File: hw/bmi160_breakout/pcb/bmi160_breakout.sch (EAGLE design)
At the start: 4 parts, among them CON1 B4B-ZR, U1 BMI160LGA14

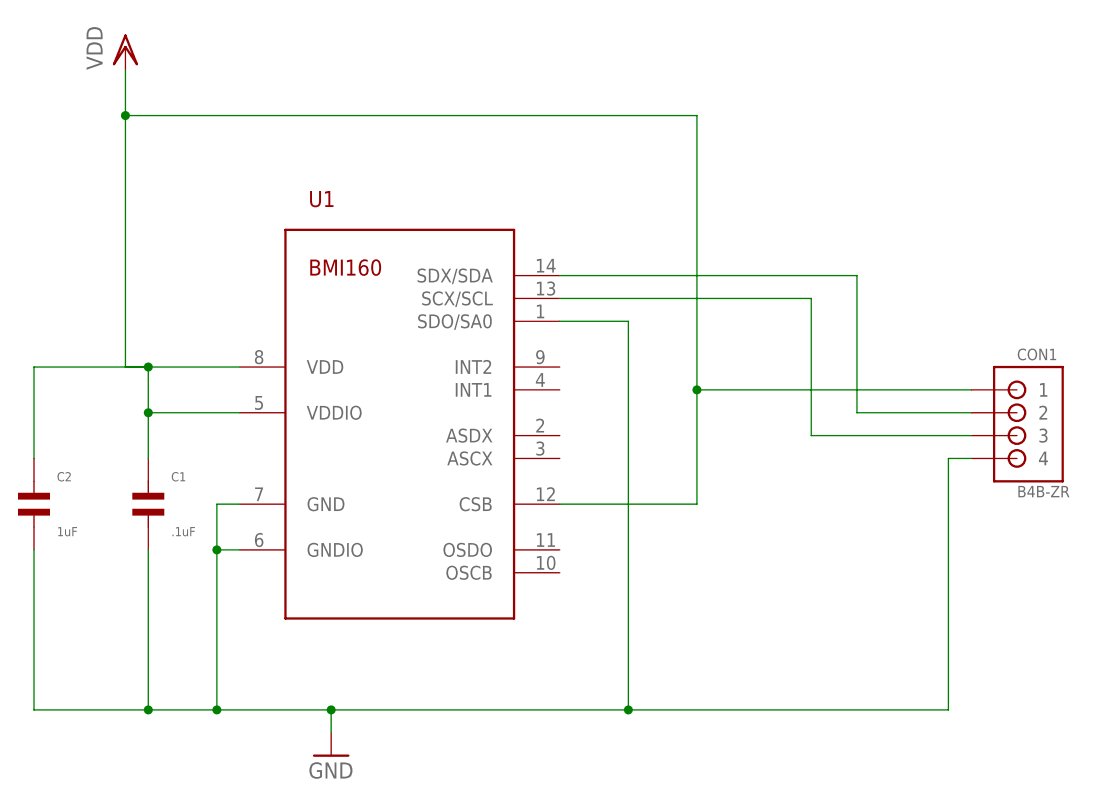
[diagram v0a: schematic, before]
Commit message: BMI160 breakout: Add a solder jumper to select I2C address.  Add silk to denote orientation.
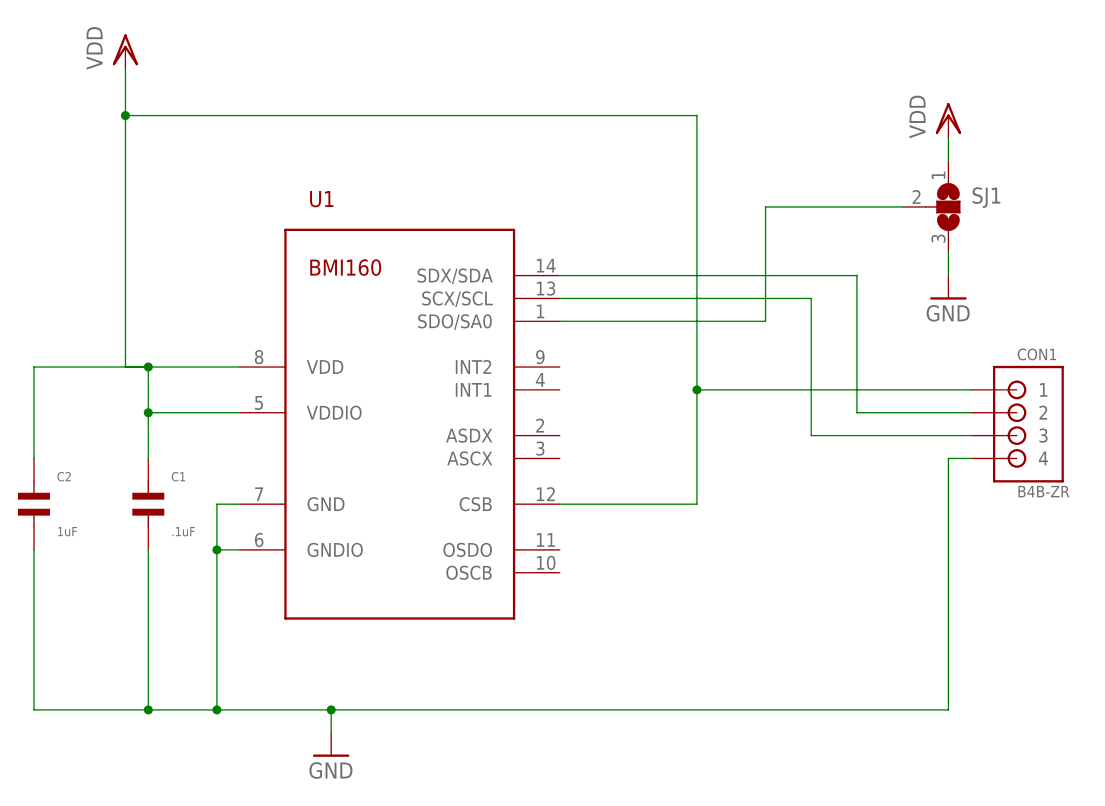
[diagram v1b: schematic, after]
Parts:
- added SJ1: (no value), jumper:SJ2W
- U1: MOUSER_PN (none) -> 262-BMI160; MPN (none) -> BMI160
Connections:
- new net N$1: SJ1.2, U1.SDO/SA0
- net GND: now also SJ1.3; no longer U1.SDO/SA0
- net VDD: now also SJ1.1
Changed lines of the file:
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@@
 </classes>
 <parts>
-<part name="U1" library="bmi160_breakout" deviceset="BMI160" device="LGA14"/>
+<part name="U1" library="bmi160_breakout" deviceset="BMI160" device="LGA14">
+<attribute name="MOUSER_PN" value="262-BMI160"/>
+<attribute name="MPN" value="BMI160"/>
+</part>
 <part name="GND1" library="supply1" deviceset="GND" device=""/>
 <part name="VDD1" library="supply1" deviceset="VDD" device=""/>
@@
 </part>
 <part name="CON1" library="bmi160_breakout" deviceset="B4B-ZR" device=""/>
+<part name="SJ1" library="jumper" deviceset="SJ2W" device=""/>
+<part name="GND2" library="supply1" deviceset="GND" device=""/>
+<part name="VDD2" library="supply1" deviceset="VDD" device=""/>
 </parts>
 <sheets>
@@
 </plain>
 <instances>
-<instance part="U1" gate="G$1" x="68.58" y="43.18"/>
+<instance part="U1" gate="G$1" x="68.58" y="43.18">
+<attribute name="MOUSER_PN" x="68.58" y="43.18" size="1.778" layer="96" display="off"/>
+<attribute name="MPN" x="68.58" y="43.18" size="1.778" layer="96" display="off"/>
+</instance>
 <instance part="GND1" gate="1" x="60.96" y="5.08"/>
 <instance part="VDD1" gate="G$1" x="38.1" y="83.82"/>
@@
 </instance>
 <instance part="CON1" gate="G$1" x="139.7" y="43.18"/>
+<instance part="SJ1" gate="G$1" x="129.54" y="66.04"/>
+<instance part="GND2" gate="1" x="129.54" y="55.88"/>
+<instance part="VDD2" gate="G$1" x="129.54" y="76.2"/>
 </instances>
 <busses>
@@
 <wire x1="27.94" y1="10.16" x2="40.64" y2="10.16" width="0.1524" layer="91"/>
 <junction x="40.64" y="10.16"/>
-<pinref part="U1" gate="G$1" pin="SDO/SA0"/>
-<wire x1="86.36" y1="53.34" x2="93.98" y2="53.34" width="0.1524" layer="91"/>
-<wire x1="93.98" y1="53.34" x2="93.98" y2="10.16" width="0.1524" layer="91"/>
-<wire x1="93.98" y1="10.16" x2="60.96" y2="10.16" width="0.1524" layer="91"/>
 <junction x="60.96" y="10.16"/>
-<wire x1="93.98" y1="10.16" x2="129.54" y2="10.16" width="0.1524" layer="91"/>
+<wire x1="60.96" y1="10.16" x2="129.54" y2="10.16" width="0.1524" layer="91"/>
 <wire x1="129.54" y1="10.16" x2="129.54" y2="38.1" width="0.1524" layer="91"/>
-<junction x="93.98" y="10.16"/>
 <pinref part="CON1" gate="G$1" pin="4"/>
 <wire x1="129.54" y1="38.1" x2="132.08" y2="38.1" width="0.1524" layer="91"/>
+</segment>
+<segment>
+<pinref part="SJ1" gate="G$1" pin="3"/>
+<pinref part="GND2" gate="1" pin="GND"/>
+<wire x1="129.54" y1="60.96" x2="129.54" y2="58.42" width="0.1524" layer="91"/>
 </segment>
 </net>
@@
 <junction x="101.6" y="45.72"/>
 </segment>
+<segment>
+<pinref part="SJ1" gate="G$1" pin="1"/>
+<pinref part="VDD2" gate="G$1" pin="VDD"/>
+<wire x1="129.54" y1="71.12" x2="129.54" y2="73.66" width="0.1524" layer="91"/>
+</segment>
 </net>
 <net name="SDA" class="0">
@@
 </segment>
 </net>
+<net name="N$1" class="0">
+<segment>
+<pinref part="U1" gate="G$1" pin="SDO/SA0"/>
+<wire x1="86.36" y1="53.34" x2="109.22" y2="53.34" width="0.1524" layer="91"/>
+<wire x1="109.22" y1="53.34" x2="109.22" y2="66.04" width="0.1524" layer="91"/>
+<pinref part="SJ1" gate="G$1" pin="2"/>
+<wire x1="109.22" y1="66.04" x2="124.46" y2="66.04" width="0.1524" layer="91"/>
+</segment>
+</net>

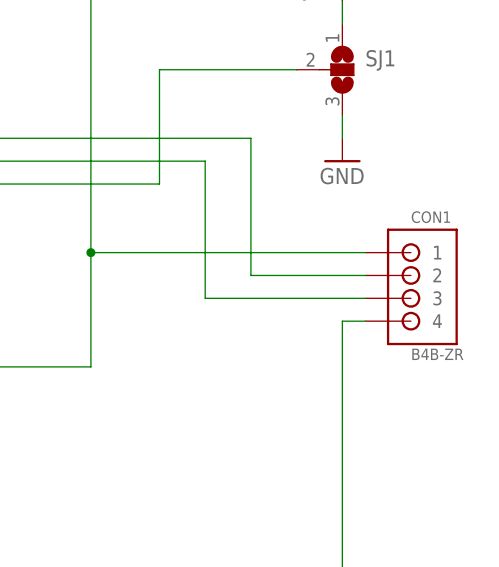
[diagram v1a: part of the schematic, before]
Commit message: bmi160 breakout: Update primary connector to 0.1" header, as it barely makes the board bigger but makes it a lot more convenient.
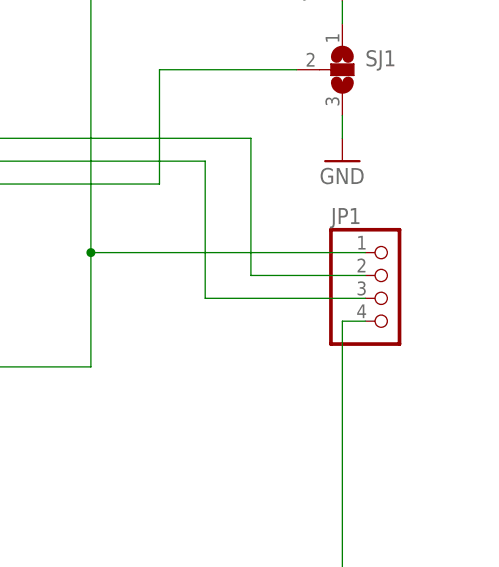
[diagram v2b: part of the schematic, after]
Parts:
- removed CON1: B4B-ZR, bmi160_breakout:B4B-ZR
- added JP1: (no value), pinhead:PINHD-1X4
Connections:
- net GND: now also JP1.4; no longer CON1.4
- net SCL: now also JP1.3; no longer CON1.3
- net SDA: now also JP1.2; no longer CON1.2
- net VDD: now also JP1.1; no longer CON1.1
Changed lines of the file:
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@@
 <attribute name="AMFPN" value="MF-CAP-0805-1uF"/>
 </part>
-<part name="CON1" library="bmi160_breakout" deviceset="B4B-ZR" device=""/>
 <part name="SJ1" library="jumper" deviceset="SJ2W" device=""/>
 <part name="GND2" library="supply1" deviceset="GND" device=""/>
 <part name="VDD2" library="supply1" deviceset="VDD" device=""/>
+<part name="JP1" library="pinhead" deviceset="PINHD-1X4" device=""/>
 </parts>
 <sheets>
@@
 <attribute name="AMFPN" x="27.94" y="33.02" size="1.778" layer="96" display="off"/>
 </instance>
-<instance part="CON1" gate="G$1" x="139.7" y="43.18"/>
 <instance part="SJ1" gate="G$1" x="129.54" y="66.04"/>
 <instance part="GND2" gate="1" x="129.54" y="55.88"/>
 <instance part="VDD2" gate="G$1" x="129.54" y="76.2"/>
+<instance part="JP1" gate="A" x="134.62" y="40.64"/>
 </instances>
 <busses>
@@
 <wire x1="60.96" y1="10.16" x2="129.54" y2="10.16" width="0.1524" layer="91"/>
 <wire x1="129.54" y1="10.16" x2="129.54" y2="38.1" width="0.1524" layer="91"/>
-<pinref part="CON1" gate="G$1" pin="4"/>
 <wire x1="129.54" y1="38.1" x2="132.08" y2="38.1" width="0.1524" layer="91"/>
+<pinref part="JP1" gate="A" pin="4"/>
 </segment>
 <segment>
@@
 <wire x1="101.6" y1="45.72" x2="101.6" y2="33.02" width="0.1524" layer="91"/>
 <wire x1="101.6" y1="33.02" x2="86.36" y2="33.02" width="0.1524" layer="91"/>
-<pinref part="CON1" gate="G$1" pin="1"/>
 <wire x1="132.08" y1="45.72" x2="101.6" y2="45.72" width="0.1524" layer="91"/>
 <junction x="101.6" y="45.72"/>
+<pinref part="JP1" gate="A" pin="1"/>
 </segment>
 <segment>
@@
 <wire x1="86.36" y1="58.42" x2="119.38" y2="58.42" width="0.1524" layer="91"/>
 <wire x1="119.38" y1="58.42" x2="119.38" y2="43.18" width="0.1524" layer="91"/>
-<pinref part="CON1" gate="G$1" pin="2"/>
 <wire x1="119.38" y1="43.18" x2="132.08" y2="43.18" width="0.1524" layer="91"/>
+<pinref part="JP1" gate="A" pin="2"/>
 </segment>
 </net>
@@
 <wire x1="86.36" y1="55.88" x2="114.3" y2="55.88" width="0.1524" layer="91"/>
 <wire x1="114.3" y1="55.88" x2="114.3" y2="40.64" width="0.1524" layer="91"/>
-<pinref part="CON1" gate="G$1" pin="3"/>
 <wire x1="114.3" y1="40.64" x2="132.08" y2="40.64" width="0.1524" layer="91"/>
+<pinref part="JP1" gate="A" pin="3"/>
 </segment>
 </net>
